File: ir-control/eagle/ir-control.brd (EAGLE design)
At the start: 40 x 45 mm, 31 parts, among them J1 MICRO USB, J2 MICRO USB, J3 MICRO USB, J4 JACKX, Q1 DTA114EET1G (2x10K), Q2 12Mhz, Q3 NPN, U1 NUF2042XV6T1G, U2 MCP1754ST-3302E/CB, U3 LPC11U35FHI33/501

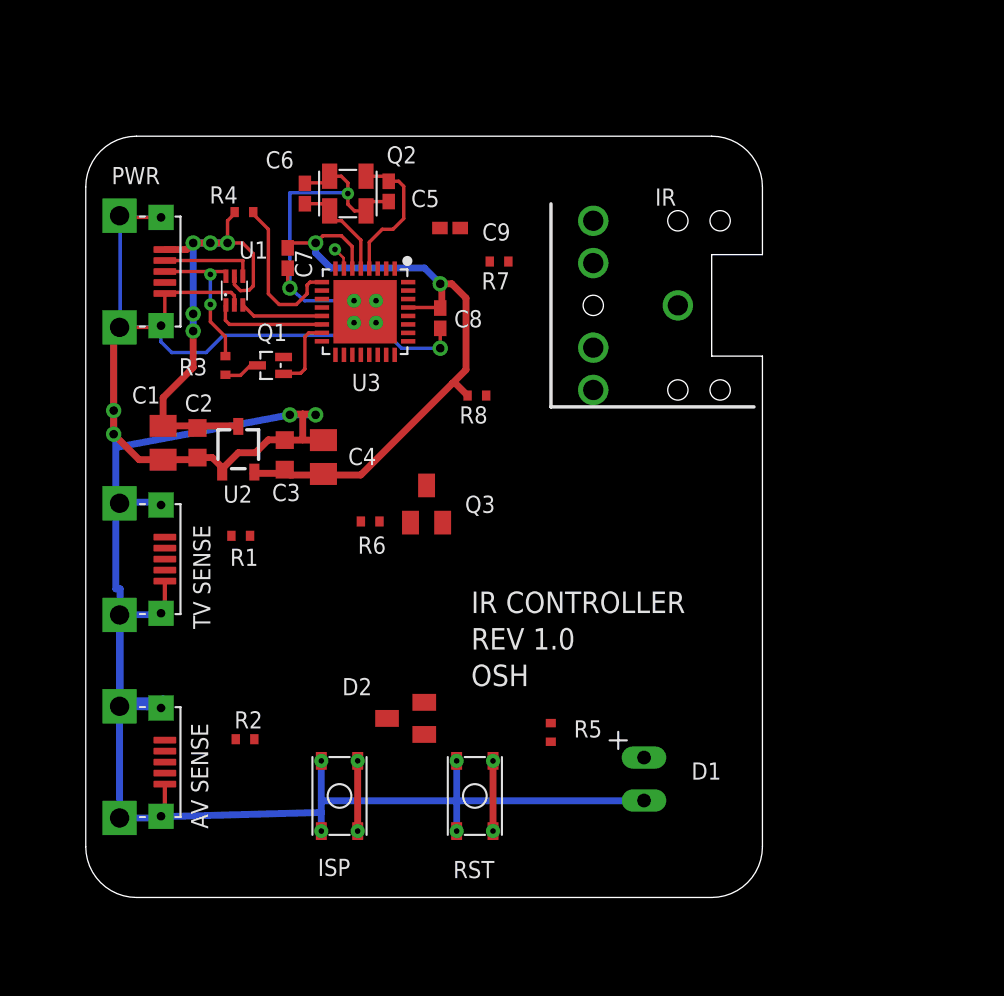
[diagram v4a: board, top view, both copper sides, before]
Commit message: Added opto couplers.
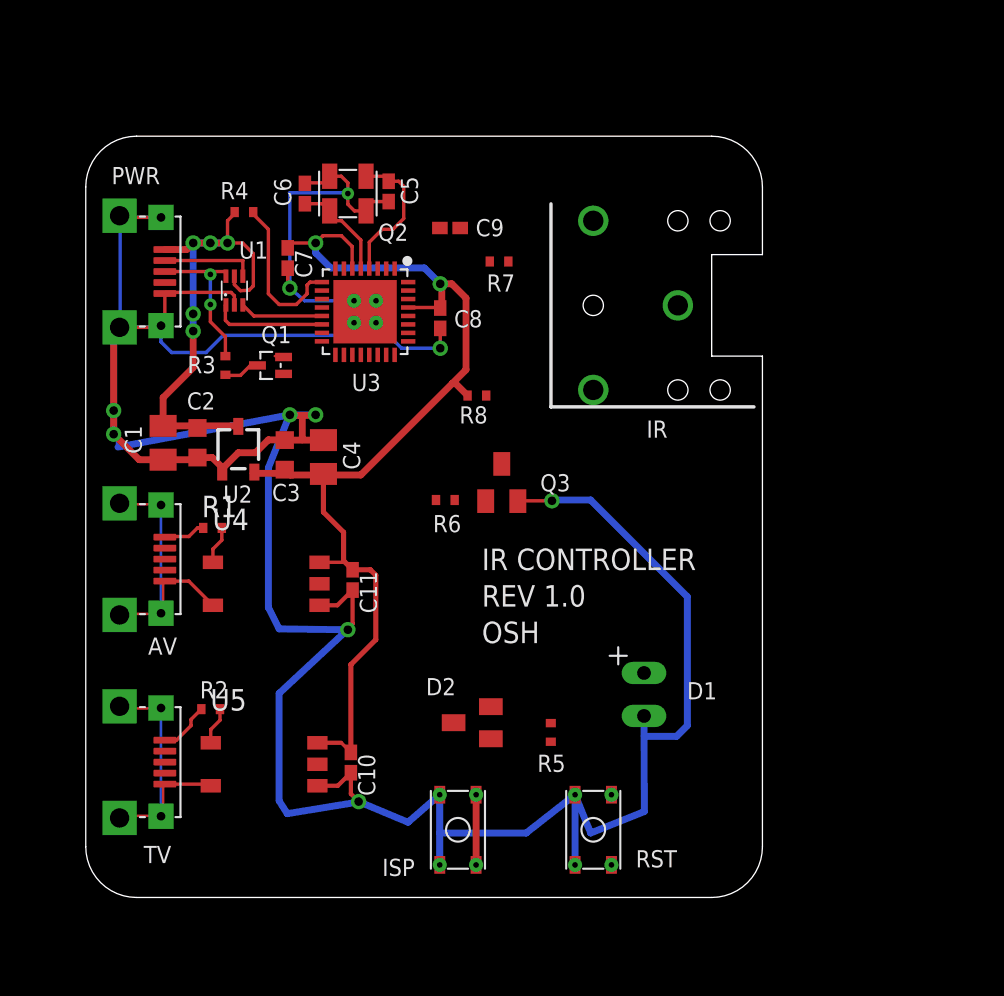
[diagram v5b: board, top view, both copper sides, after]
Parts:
- added C10, C11: 0.1uF, ir-control:C0402K
- added U4, U5: TLP2361, ir-control:SO6
- J4: value JACKX -> SJ1-3523NG
- R1, R2: value 10K -> 1K5
- moved S1 7.28 mm to (22.0, 4.00)
- moved S2 7.28 mm to (30.0, 4.00)
- moved D1 5.00 mm to (33.0, 12.0)
- moved Q3 4.62 mm to (24.6, 24.5)
- moved R6 4.62 mm to (21.3, 23.5)
- moved D2 3.95 mm to (22.8, 10.3)
- moved R2 2.70 mm to (7.38, 11.1)
- moved R1 1.73 mm to (7.49, 21.8)
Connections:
- removed net AV_SENSE: R2.2, U3.21
- removed net TV_SENSE: R1.2, U3.19
- new net !AV_ON: U3.19, U4.5
- new net !TV_ON: U3.21, U5.5
- new net N$10: J2.5, J2.G1, J2.G2, J2.G3, J2.G4, U4.3
- new net N$11: J1.5, J1.G1, J1.G2, J1.G3, J1.G4, U5.3
- new net N$13: R2.2, U5.1
- new net N$15: R1.2, U4.1
- net +3V3: now also C10.1, C11.1, U4.6, U5.6
- net GND: now also C10.2, C11.2, U4.4, U5.4; no longer J1.5, J1.G1, J1.G2, J1.G3, J1.G4, J2.5, J2.G1, J2.G2, J2.G3, J2.G4
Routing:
- net +3V3: track 40.5 -> 64.3 mm
- net GND: track 199.4 -> 219.3 mm, vias 7 -> 10
- net N$10: track 0.00 -> 16.9 mm
- net N$11: track 0.00 -> 16.3 mm
- net !USB_CONNECT: track 4.39 -> 0.00 mm
- net !RESET: track 4.15 -> 0.00 mm
- net N$7: track 0.00 -> 3.13 mm
- net N$2: track 0.00 -> 2.49 mm
- net N$15: track 0.00 -> 2.25 mm
- net N$13: track 0.00 -> 2.21 mm
- net LED: track 1.35 -> 0.00 mm, vias 1 -> 0
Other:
- board text added: "AV"
- board text added: "TV"
- board text removed: "AV SENSE"
- board text removed: "TV SENSE"

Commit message: Minor tweaks.
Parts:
- Q3: value NPN -> MMBT2222A
- S1: value PUSH-BUTTON -> CKN10502CT-ND
- moved R5 0.63 mm to (27.5, 10.4)

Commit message: Removed the shield connection of the sense connectors.
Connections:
- net N$10: no longer J2.G1, J2.G2, J2.G3, J2.G4
- net N$11: no longer J1.G1, J1.G2, J1.G3, J1.G4
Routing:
- net N$11: track 16.3 -> 2.90 mm
- net N$10: track 16.9 -> 3.54 mm
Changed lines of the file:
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@@
 <signal name="N$11">
 <contactref element="J1" pad="5"/>
-<contactref element="J1" pad="G2"/>
-<contactref element="J1" pad="G3"/>
-<contactref element="J1" pad="G4"/>
-<contactref element="J1" pad="G1"/>
 <contactref element="U5" pad="3"/>
 <wire x1="4.675" y1="6.7" x2="7.295" y2="6.7" width="0.2032" layer="1"/>
 <wire x1="7.295" y1="6.7" x2="7.391" y2="6.604" width="0.2032" layer="1"/>
-<wire x1="4.572" y1="4.826" x2="4.572" y2="6.604" width="0.1524" layer="1"/>
+<wire x1="4.572" y1="4.826" x2="4.572" y2="6.604" width="0" layer="19" extent="1-16"/>
 <wire x1="4.572" y1="6.604" x2="4.675" y2="6.7" width="0.1524" layer="1"/>
-<wire x1="4.572" y1="4.826" x2="4.45" y2="4.8" width="0.1524" layer="1"/>
-<wire x1="2.032" y1="4.826" x2="4.445" y2="4.826" width="0.1524" layer="1"/>
-<wire x1="4.445" y1="4.826" x2="4.45" y2="4.8" width="0.1524" layer="1"/>
-<wire x1="2.032" y1="4.826" x2="2" y2="4.7" width="0.1524" layer="1"/>
-<wire x1="2.032" y1="11.176" x2="4.445" y2="11.176" width="0.1524" layer="1"/>
-<wire x1="4.445" y1="11.176" x2="4.45" y2="11.2" width="0.1524" layer="1"/>
-<wire x1="2.032" y1="11.176" x2="2" y2="11.3" width="0.1524" layer="1"/>
-<wire x1="4.445" y1="11.176" x2="4.445" y2="4.826" width="0.1524" layer="16"/>
-<wire x1="4.445" y1="4.826" x2="4.45" y2="4.8" width="0.1524" layer="16"/>
-<wire x1="4.445" y1="11.176" x2="4.45" y2="11.2" width="0.1524" layer="16"/>
+<wire x1="4.572" y1="4.826" x2="4.45" y2="4.8" width="0" layer="19" extent="1-16"/>
+<wire x1="2.032" y1="4.826" x2="4.445" y2="4.826" width="0" layer="19" extent="1-16"/>
+<wire x1="4.445" y1="4.826" x2="4.45" y2="4.8" width="0" layer="19" extent="1-16"/>
+<wire x1="2.032" y1="4.826" x2="2" y2="4.7" width="0" layer="19" extent="1-16"/>
+<wire x1="2.032" y1="11.176" x2="4.445" y2="11.176" width="0" layer="19" extent="1-16"/>
+<wire x1="4.445" y1="11.176" x2="4.45" y2="11.2" width="0" layer="19" extent="1-16"/>
+<wire x1="2.032" y1="11.176" x2="2" y2="11.3" width="0" layer="19" extent="1-16"/>
+<wire x1="4.445" y1="11.176" x2="4.445" y2="4.826" width="0" layer="19" extent="1-16"/>
+<wire x1="4.445" y1="4.826" x2="4.45" y2="4.8" width="0" layer="19" extent="1-16"/>
+<wire x1="4.445" y1="11.176" x2="4.45" y2="11.2" width="0" layer="19" extent="1-16"/>
 </signal>
 <signal name="N$13">
@@
 <contactref element="U4" pad="3"/>
 <contactref element="J2" pad="5"/>
-<contactref element="J2" pad="G2"/>
-<contactref element="J2" pad="G3"/>
-<contactref element="J2" pad="G4"/>
-<contactref element="J2" pad="G1"/>
 <wire x1="4.675" y1="18.7" x2="6.09" y2="18.7" width="0.2032" layer="1"/>
 <wire x1="6.09" y1="18.7" x2="7.518" y2="17.272" width="0.2032" layer="1"/>
-<wire x1="4.572" y1="16.891" x2="4.572" y2="18.669" width="0.1524" layer="1"/>
+<wire x1="4.572" y1="16.891" x2="4.572" y2="18.669" width="0" layer="19" extent="1-16"/>
 <wire x1="4.572" y1="18.669" x2="4.675" y2="18.7" width="0.1524" layer="1"/>
-<wire x1="4.572" y1="16.891" x2="4.45" y2="16.8" width="0.1524" layer="1"/>
-<wire x1="2.032" y1="16.764" x2="4.445" y2="16.764" width="0.1524" layer="1"/>
-<wire x1="4.445" y1="16.764" x2="4.45" y2="16.8" width="0.1524" layer="1"/>
-<wire x1="2.032" y1="16.764" x2="2" y2="16.7" width="0.1524" layer="1"/>
-<wire x1="2.032" y1="23.241" x2="4.445" y2="23.241" width="0.1524" layer="1"/>
-<wire x1="4.445" y1="23.241" x2="4.45" y2="23.2" width="0.1524" layer="1"/>
-<wire x1="2.032" y1="23.241" x2="2" y2="23.3" width="0.1524" layer="1"/>
-<wire x1="4.445" y1="23.114" x2="4.445" y2="16.891" width="0.1524" layer="16"/>
-<wire x1="4.445" y1="16.891" x2="4.45" y2="16.8" width="0.1524" layer="16"/>
-<wire x1="4.445" y1="23.114" x2="4.45" y2="23.2" width="0.1524" layer="16"/>
+<wire x1="4.572" y1="16.891" x2="4.45" y2="16.8" width="0" layer="19" extent="1-16"/>
+<wire x1="2.032" y1="16.764" x2="4.445" y2="16.764" width="0" layer="19" extent="1-16"/>
+<wire x1="4.445" y1="16.764" x2="4.45" y2="16.8" width="0" layer="19" extent="1-16"/>
+<wire x1="2.032" y1="16.764" x2="2" y2="16.7" width="0" layer="19" extent="1-16"/>
+<wire x1="2.032" y1="23.241" x2="4.445" y2="23.241" width="0" layer="19" extent="1-16"/>
+<wire x1="4.445" y1="23.241" x2="4.45" y2="23.2" width="0" layer="19" extent="1-16"/>
+<wire x1="2.032" y1="23.241" x2="2" y2="23.3" width="0" layer="19" extent="1-16"/>
+<wire x1="4.445" y1="23.114" x2="4.445" y2="16.891" width="0" layer="19" extent="1-16"/>
+<wire x1="4.445" y1="16.891" x2="4.45" y2="16.8" width="0" layer="19" extent="1-16"/>
+<wire x1="4.445" y1="23.114" x2="4.45" y2="23.2" width="0" layer="19" extent="1-16"/>
 </signal>
 <signal name="N$15">

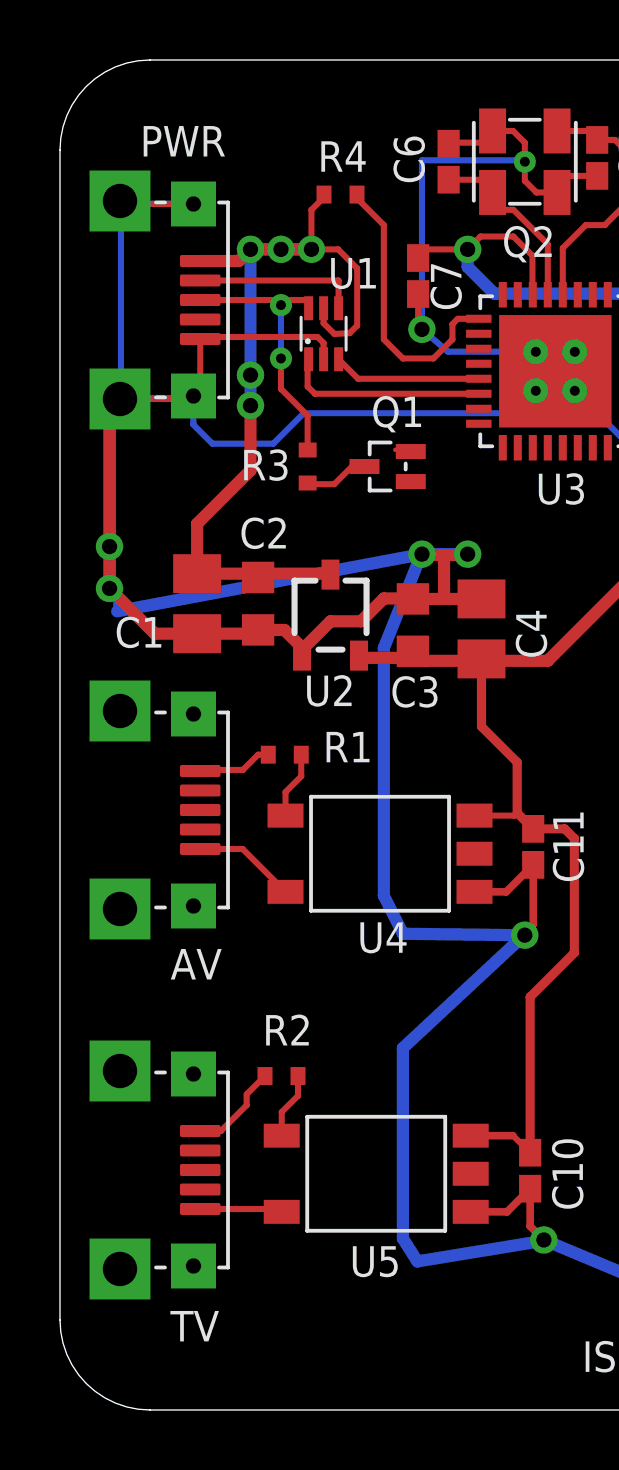
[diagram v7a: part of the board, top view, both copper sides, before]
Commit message: Removed connection to av/tv shields.
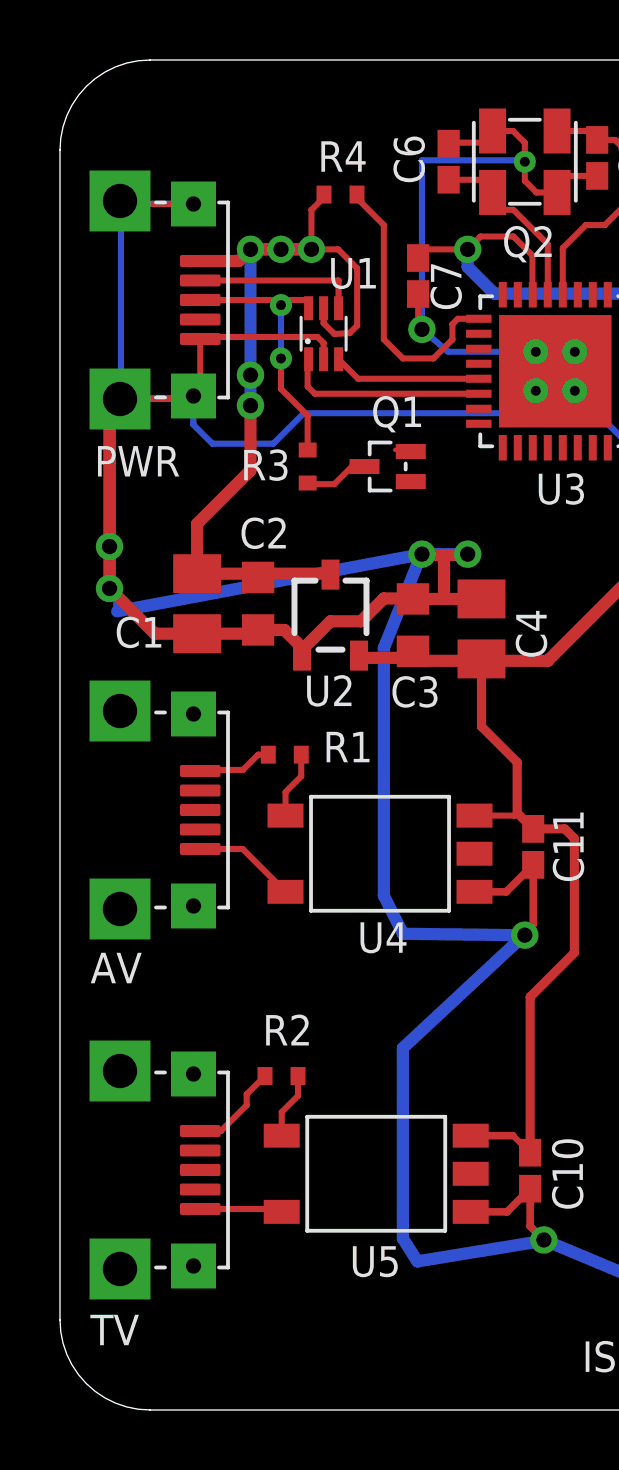
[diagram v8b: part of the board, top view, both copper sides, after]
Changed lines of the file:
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@@
 <text x="17.399" y="1.27" size="1.016" layer="21" font="vector" ratio="10">ISP</text>
 <text x="32.512" y="1.27" size="1.016" layer="21" font="vector" ratio="10">RST</text>
-<text x="3.683" y="2.286" size="1.016" layer="21" font="vector" ratio="10">TV</text>
-<text x="3.683" y="14.351" size="1.016" layer="21" font="vector" ratio="10">AV</text>
-<text x="2.667" y="41.783" size="1.016" layer="21" font="vector" ratio="10">PWR</text>
+<text x="1.016" y="2.159" size="1.016" layer="21" font="vector" ratio="10">TV</text>
+<text x="1.016" y="14.224" size="1.016" layer="21" font="vector" ratio="10">AV</text>
+<text x="1.143" y="31.115" size="1.016" layer="21" font="vector" ratio="10">PWR</text>
 <rectangle x1="-0.381" y1="33.274" x2="0.762" y2="41.148" layer="41"/>
 <rectangle x1="-0.381" y1="16.129" x2="0.762" y2="24.003" layer="41"/>
@@
 <wire x1="22.479" y1="31.195" x2="22.479" y2="35.433" width="0.4064" layer="1"/>
 <wire x1="22.479" y1="35.433" x2="21.637" y2="36.275" width="0.4064" layer="1"/>
-<wire x1="21.971" y1="35.941" x2="21.637" y2="36.275" width="0" layer="19" extent="1-16"/>
 <wire x1="21.637" y1="36.275" x2="20.955" y2="36.275" width="0.4064" layer="1"/>
 <wire x1="22.571" y1="29.669" x2="21.847" y2="30.393" width="0.4064" layer="1"/>
@@
 <wire x1="15.148" y1="19.812" x2="13.818" y2="19.812" width="0.2032" layer="1"/>
 <wire x1="15.1034" y1="9.144" x2="15.6718" y2="8.5756" width="0.2032" layer="1"/>
-<wire x1="22.098" y1="36.068" x2="22.098" y2="39.497" width="0" layer="19" extent="1-16"/>
 <wire x1="22.098" y1="39.497" x2="22.134" y2="39.573" width="0.1524" layer="1"/>
-<wire x1="22.098" y1="36.068" x2="21.971" y2="35.941" width="0" layer="19" extent="1-16"/>
 <wire x1="11.176" y1="32.004" x2="11.684" y2="32.004" width="0.1524" layer="1"/>
 <wire x1="11.684" y1="32.004" x2="11.693" y2="31.949" width="0.1524" layer="1"/>
@@
 <wire x1="14.097" y1="25.019" x2="14.097" y2="24.972" width="0.1524" layer="1"/>
 <wire x1="14.097" y1="25.019" x2="14.05" y2="25.035" width="0.1524" layer="1"/>
-<wire x1="14.478" y1="37.211" x2="11.684" y2="32.004" width="0" layer="19" extent="1-16"/>
+<wire x1="20.019" y1="37.211" x2="22.098" y2="39.497" width="0" layer="19" extent="1-16"/>
+<wire x1="11.684" y1="32.004" x2="14.478" y2="37.211" width="0" layer="19" extent="1-16"/>
 </signal>
 <signal name="!USB_CONNECT">
@@
 <contactref element="D2" pad="2"/>
 <contactref element="U3" pad="3"/>
-<wire x1="17.272" y1="37.719" x2="17.272" y2="37.211" width="0" layer="19" extent="1-16"/>
-<wire x1="19.05" y1="39.497" x2="17.272" y2="37.719" width="0" layer="19" extent="1-16"/>
-<wire x1="20.828" y1="39.497" x2="19.05" y2="39.497" width="0" layer="19" extent="1-16"/>
 <wire x1="17.272" y1="37.211" x2="17.26" y2="37.174" width="0.1524" layer="1"/>
 <wire x1="20.828" y1="39.497" x2="20.934" y2="39.573" width="0.1524" layer="1"/>
+<wire x1="17.272" y1="37.211" x2="20.828" y2="39.497" width="0" layer="19" extent="1-1"/>
 <wire x1="23.946" y1="11.281" x2="17.26" y2="37.174" width="0" layer="19" extent="1-1"/>
 </signal>
@@
 <contactref element="R6" pad="1"/>
 <contactref element="Q3" pad="1"/>
-<wire x1="23.622" y1="23.495" x2="21.806" y2="23.495" width="0" layer="19" extent="1-16"/>
 <wire x1="23.622" y1="23.495" x2="23.641" y2="23.427" width="0.1524" layer="1"/>
+<wire x1="21.806" y1="23.495" x2="23.622" y2="23.495" width="0" layer="19" extent="1-1"/>
 </signal>
 <signal name="IR">
@@
 <wire x1="4.675" y1="6.7" x2="7.295" y2="6.7" width="0.2032" layer="1"/>
 <wire x1="7.295" y1="6.7" x2="7.391" y2="6.604" width="0.2032" layer="1"/>
-<wire x1="4.572" y1="4.826" x2="4.572" y2="6.604" width="0" layer="19" extent="1-16"/>
 <wire x1="4.572" y1="6.604" x2="4.675" y2="6.7" width="0.1524" layer="1"/>
-<wire x1="4.572" y1="4.826" x2="4.45" y2="4.8" width="0" layer="19" extent="1-16"/>
-<wire x1="2.032" y1="4.826" x2="4.445" y2="4.826" width="0" layer="19" extent="1-16"/>
-<wire x1="4.445" y1="4.826" x2="4.45" y2="4.8" width="0" layer="19" extent="1-16"/>
-<wire x1="2.032" y1="4.826" x2="2" y2="4.7" width="0" layer="19" extent="1-16"/>
-<wire x1="2.032" y1="11.176" x2="4.445" y2="11.176" width="0" layer="19" extent="1-16"/>
-<wire x1="4.445" y1="11.176" x2="4.45" y2="11.2" width="0" layer="19" extent="1-16"/>
-<wire x1="2.032" y1="11.176" x2="2" y2="11.3" width="0" layer="19" extent="1-16"/>
-<wire x1="4.445" y1="11.176" x2="4.445" y2="4.826" width="0" layer="19" extent="1-16"/>
-<wire x1="4.445" y1="4.826" x2="4.45" y2="4.8" width="0" layer="19" extent="1-16"/>
-<wire x1="4.445" y1="11.176" x2="4.45" y2="11.2" width="0" layer="19" extent="1-16"/>
 </signal>
 <signal name="N$13">
@@
 <wire x1="4.675" y1="18.7" x2="6.09" y2="18.7" width="0.2032" layer="1"/>
 <wire x1="6.09" y1="18.7" x2="7.518" y2="17.272" width="0.2032" layer="1"/>
-<wire x1="4.572" y1="16.891" x2="4.572" y2="18.669" width="0" layer="19" extent="1-16"/>
 <wire x1="4.572" y1="18.669" x2="4.675" y2="18.7" width="0.1524" layer="1"/>
-<wire x1="4.572" y1="16.891" x2="4.45" y2="16.8" width="0" layer="19" extent="1-16"/>
-<wire x1="2.032" y1="16.764" x2="4.445" y2="16.764" width="0" layer="19" extent="1-16"/>
-<wire x1="4.445" y1="16.764" x2="4.45" y2="16.8" width="0" layer="19" extent="1-16"/>
-<wire x1="2.032" y1="16.764" x2="2" y2="16.7" width="0" layer="19" extent="1-16"/>
-<wire x1="2.032" y1="23.241" x2="4.445" y2="23.241" width="0" layer="19" extent="1-16"/>
-<wire x1="4.445" y1="23.241" x2="4.45" y2="23.2" width="0" layer="19" extent="1-16"/>
-<wire x1="2.032" y1="23.241" x2="2" y2="23.3" width="0" layer="19" extent="1-16"/>
-<wire x1="4.445" y1="23.114" x2="4.445" y2="16.891" width="0" layer="19" extent="1-16"/>
-<wire x1="4.445" y1="16.891" x2="4.45" y2="16.8" width="0" layer="19" extent="1-16"/>
-<wire x1="4.445" y1="23.114" x2="4.45" y2="23.2" width="0" layer="19" extent="1-16"/>
 </signal>
 <signal name="N$15">
